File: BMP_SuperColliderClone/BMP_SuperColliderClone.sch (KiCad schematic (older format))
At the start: 63 parts, among them J1 BARREL_JACK, Q1 MMBT3904, Q2 MMBT3904, Q3 MMBT3904, Q4 MMBT3904

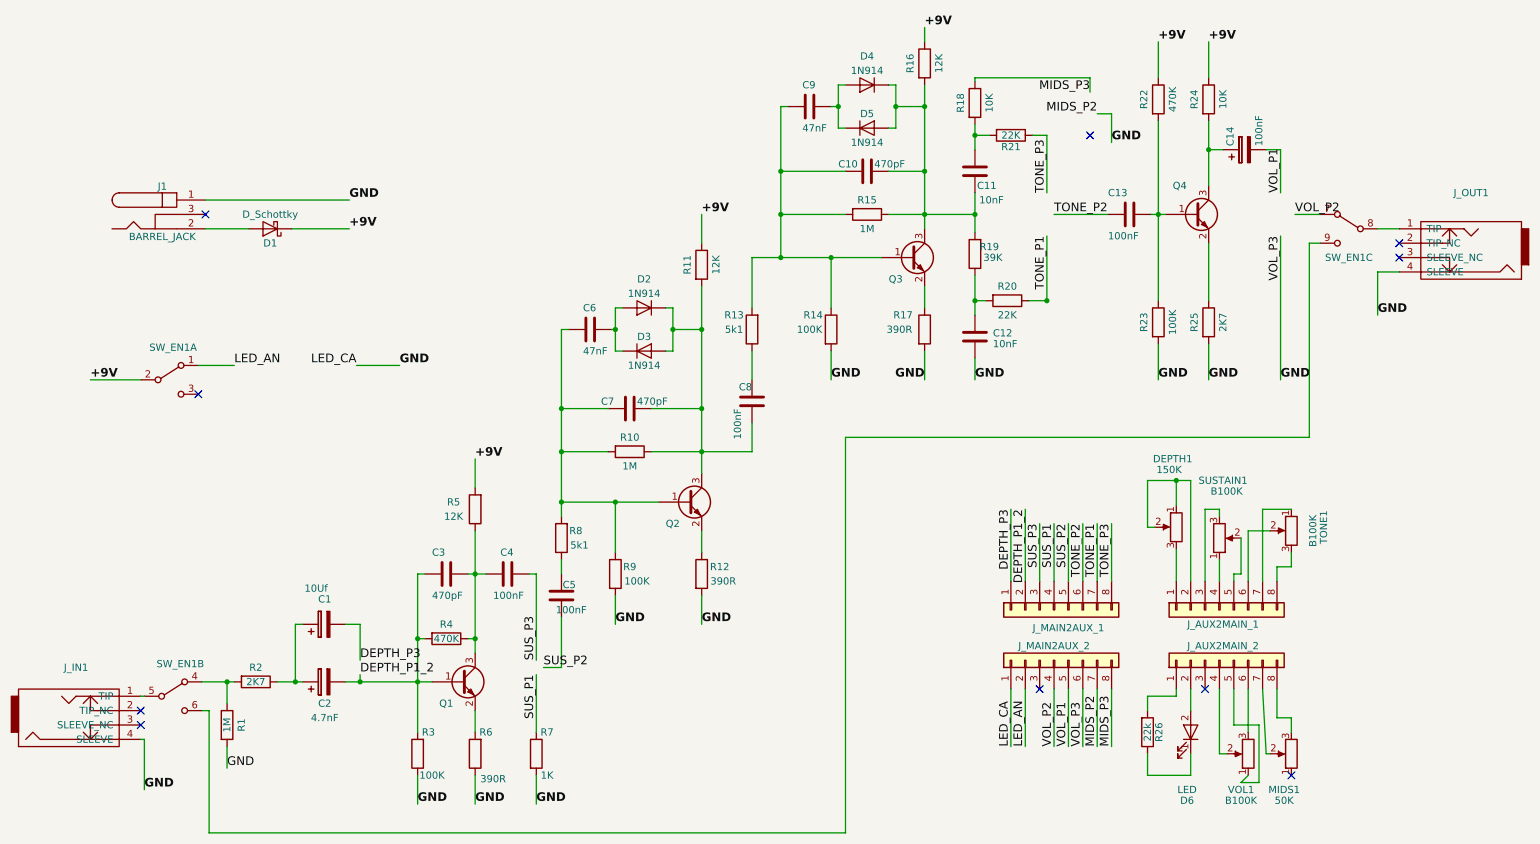
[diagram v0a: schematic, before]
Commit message: Added SuperCollidfer ModPins
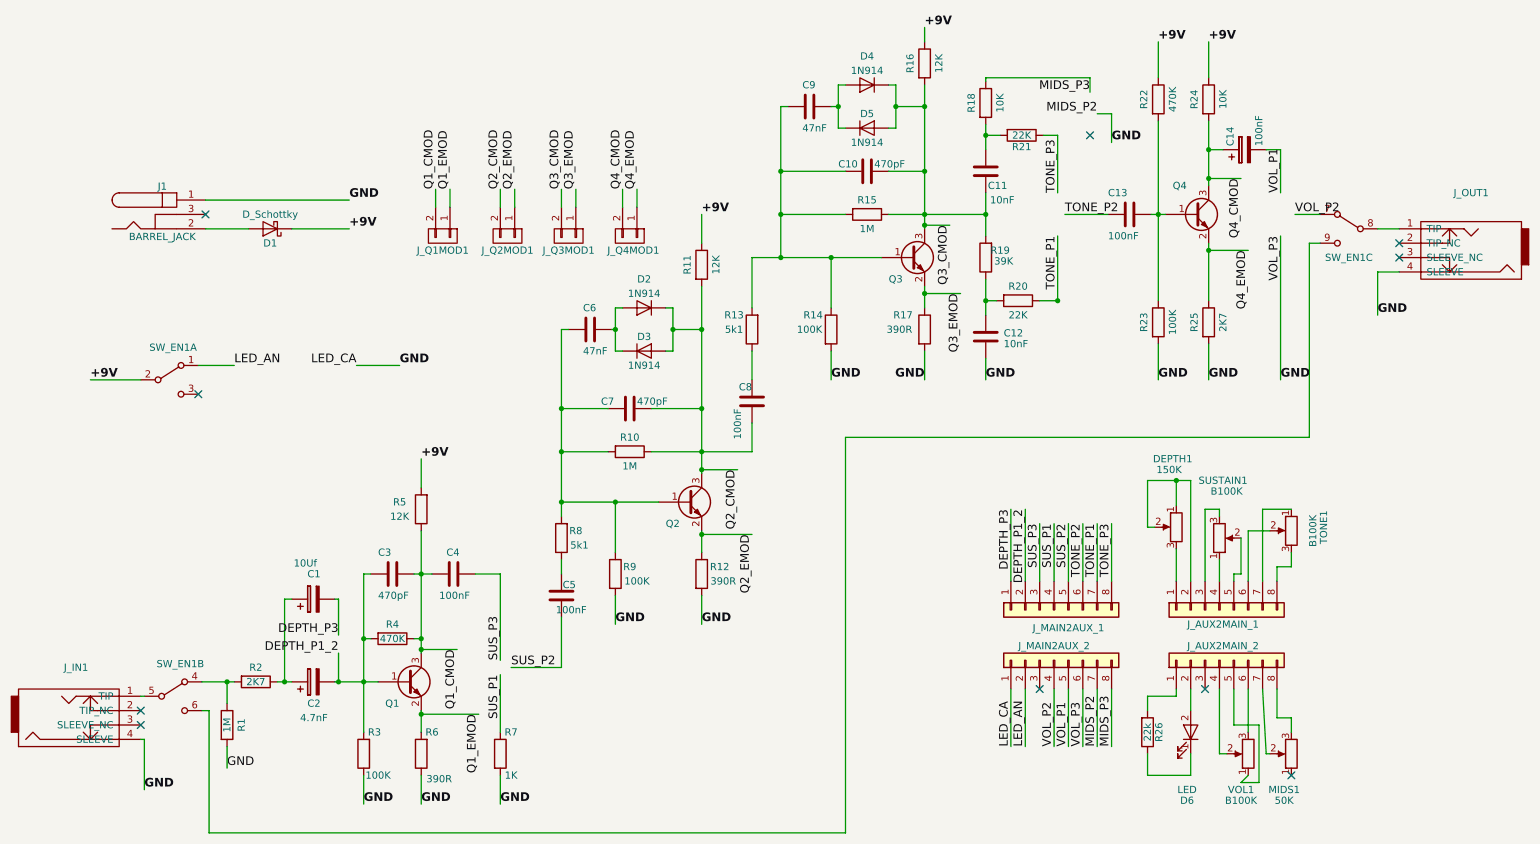
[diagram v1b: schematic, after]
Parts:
- added J_Q1MOD1, J_Q2MOD1, J_Q3MOD1, J_Q4MOD1: CONN_01X02, Pin_Headers:Pin_Header_Straight_1x02_Pitch2.54mm, symbol CONN_01X02
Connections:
- net Q1_CMOD: now reaches C3.1, C4.2, Q1.3 (C), R4.1, R5.1
- net Q1_CMOD: now also J_Q1MOD1.2 (P2)
- net Q1_EMOD: now reaches Q1.2 (E), R6.2
- net Q1_EMOD: now also J_Q1MOD1.1 (P1)
- net Q2_CMOD: now reaches C7.1, C8.1, D2.1 (K), D3.2 (A), Q2.3 (C), R10.1, R11.2
- net Q2_CMOD: now also J_Q2MOD1.2 (P2)
- net Q2_EMOD: now reaches Q2.2 (E), R12.1
- net Q2_EMOD: now also J_Q2MOD1.1 (P1)
- net Q3_CMOD: now reaches C10.1, C11.1, D4.1 (K), D5.2 (A), Q3.3 (C), R15.1, R16.2, R19.2
- net Q3_CMOD: now also J_Q3MOD1.2 (P2)
- net Q3_EMOD: now reaches Q3.2 (E), R17.1
- net Q3_EMOD: now also J_Q3MOD1.1 (P1)
- net Q4_EMOD: now reaches Q4.2 (E), R25.1
- net Q4_EMOD: now also J_Q4MOD1.1 (P1)
- net Q4_CMOD: now reaches C14.1, Q4.3 (C), R24.2
- net Q4_CMOD: now also J_Q4MOD1.2 (P2)
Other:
- moved on the sheet: C1, C11, C12, C2, C3, C4, Q1, R18, R19, R20, R21, R3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

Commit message: Added THT diodes to supercollider
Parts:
- D2, D3, D4, D5: footprint Diodes_SMD:D_SOD-123 -> Diodes_THT:D_DO-35_SOD27_P7.62mm_Horizontal
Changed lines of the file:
@@
 F 0 "D3" H 4900 3300 50  0000 C CNN
 F 1 "1N914" H 4900 3100 50  0000 C CNN
-F 2 "Diodes_SMD:D_SOD-123" H 4900 3200 50  0001 C CNN
+F 2 "Diodes_THT:D_DO-35_SOD27_P7.62mm_Horizontal" H 4900 3200 50  0001 C CNN
 F 3 "" H 4900 3200 50  0001 C CNN
 	1    4900 3200
@@
 F 0 "D2" H 4900 2700 50  0000 C CNN
 F 1 "1N914" H 4900 2800 50  0000 C CNN
-F 2 "Diodes_SMD:D_SOD-123" H 4900 2900 50  0001 C CNN
+F 2 "Diodes_THT:D_DO-35_SOD27_P7.62mm_Horizontal" H 4900 2900 50  0001 C CNN
 F 3 "" H 4900 2900 50  0001 C CNN
 	1    4900 2900
@@
 F 0 "D5" H 6450 1750 50  0000 C CNN
 F 1 "1N914" H 6450 1550 50  0000 C CNN
-F 2 "Diodes_SMD:D_SOD-123" H 6450 1650 50  0001 C CNN
+F 2 "Diodes_THT:D_DO-35_SOD27_P7.62mm_Horizontal" H 6450 1650 50  0001 C CNN
 F 3 "" H 6450 1650 50  0001 C CNN
 	1    6450 1650
@@
 F 0 "D4" H 6450 1150 50  0000 C CNN
 F 1 "1N914" H 6450 1250 50  0000 C CNN
-F 2 "Diodes_SMD:D_SOD-123" H 6450 1350 50  0001 C CNN
+F 2 "Diodes_THT:D_DO-35_SOD27_P7.62mm_Horizontal" H 6450 1350 50  0001 C CNN
 F 3 "" H 6450 1350 50  0001 C CNN
 	1    6450 1350

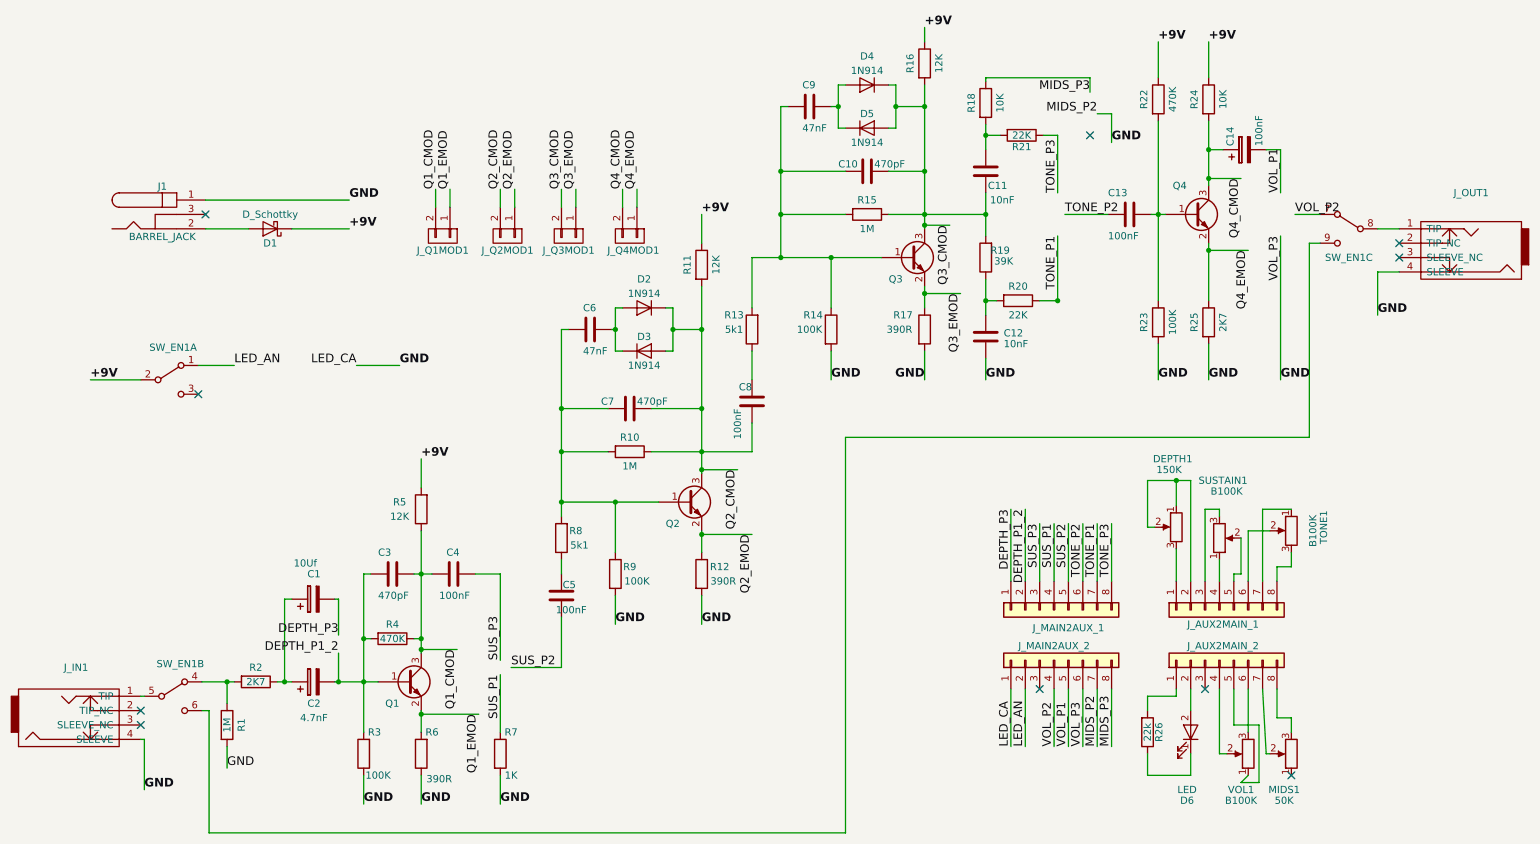
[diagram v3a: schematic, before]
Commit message: updated supercollider
- reversed polarity for sustain and depth pots
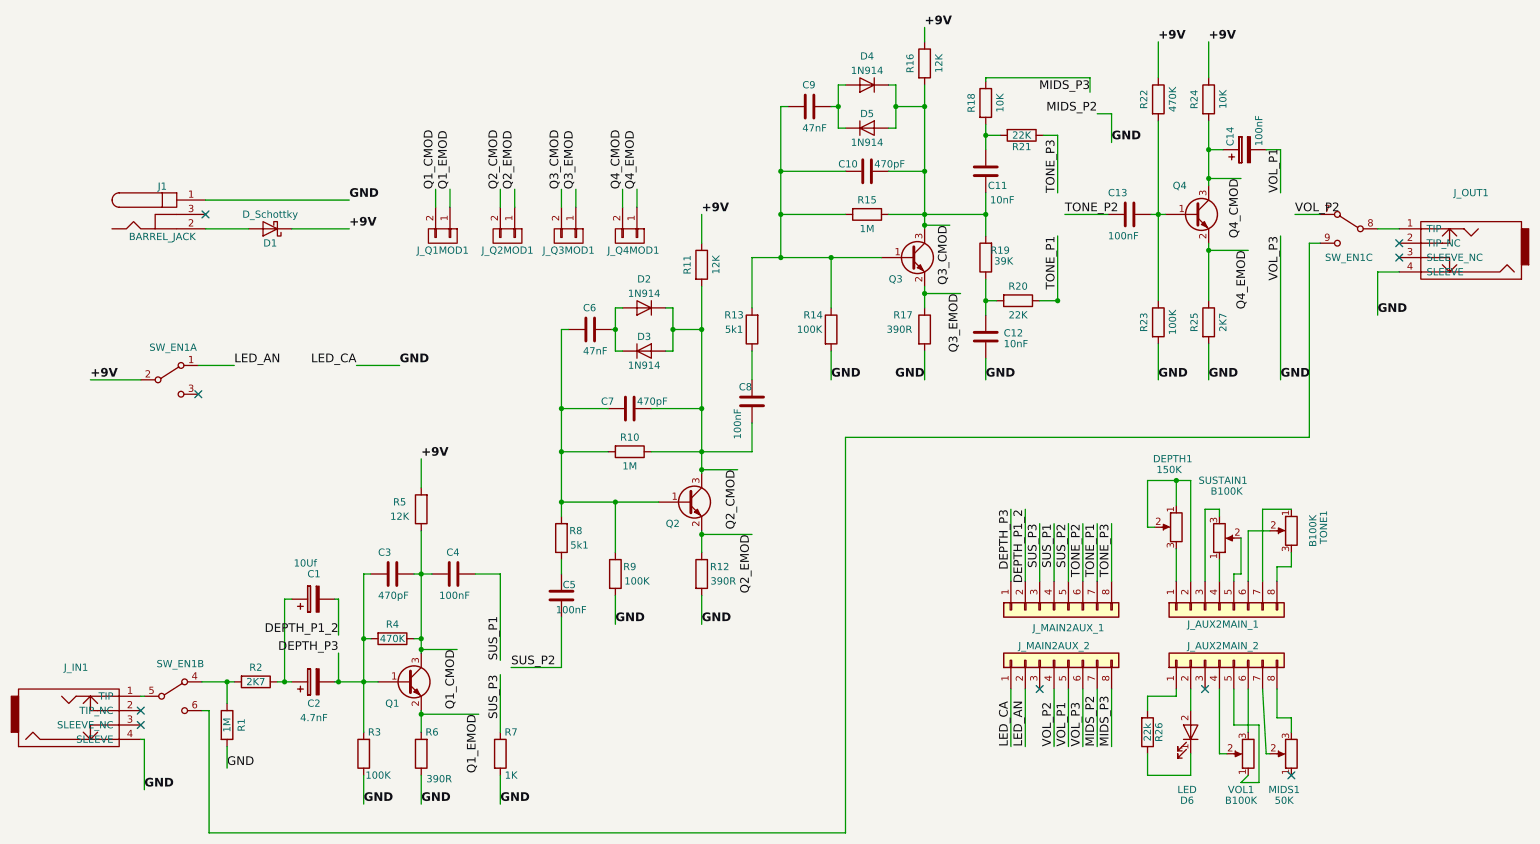
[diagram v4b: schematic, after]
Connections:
- net DEPTH_P1_2: now also C1.2; no longer C2.2, C3.2, Q1.1 (B), R3.2, R4.2
- net DEPTH_P3: now also C2.2, C3.2, Q1.1 (B), R3.2, R4.2; no longer C1.2
- net SUS_P1: now also C4.1; no longer R7.1
- net SUS_P3: now also R7.1; no longer C4.1
- no-connect marks 10 -> 9
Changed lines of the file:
@@
 Comp ""
 Comment1 ""
-Comment2 "Revision 1"
+Comment2 "Revision 2"
 Comment3 "Original Design by Earthbound Audio"
 Comment4 "SuperCollider (Big Muff Clone)"
@@
 	1    0    0    -1
 $EndComp
+Text Label 3900 5350 1    60   ~ 0
+SUS_P1
 Text Label 3900 5450 3    60   ~ 0
-SUS_P1
-Text Label 3900 5350 1    60   ~ 0
 SUS_P3
 Text Label 3975 5400 0    60   ~ 0
@@
 Wire Wire Line
 	8000 1300 8000 1400
-NoConn ~ 8000 1700
 $Comp
 L NPOT SUSTAIN1
@@
 Text Label 2000 6100 0    60   ~ 0
 GND
+Text Label 2775 5300 2    60   ~ 0
+DEPTH_P3
 Text Label 2775 5175 2    60   ~ 0
-DEPTH_P3
-Text Label 2775 5300 2    60   ~ 0
 DEPTH_P1_2
 Wire Wire Line
